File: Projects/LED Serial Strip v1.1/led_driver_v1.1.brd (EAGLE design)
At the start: 64.5 x 53.3 mm, 97 parts, among them U1 TLC5947DAP, U2 TLC5947DAP, U3 74LS595D, U4 UDN2982SLW, U5 74LS595D, U6 UDN2982SLW, U7 ARDUINO_R3_SHIELD

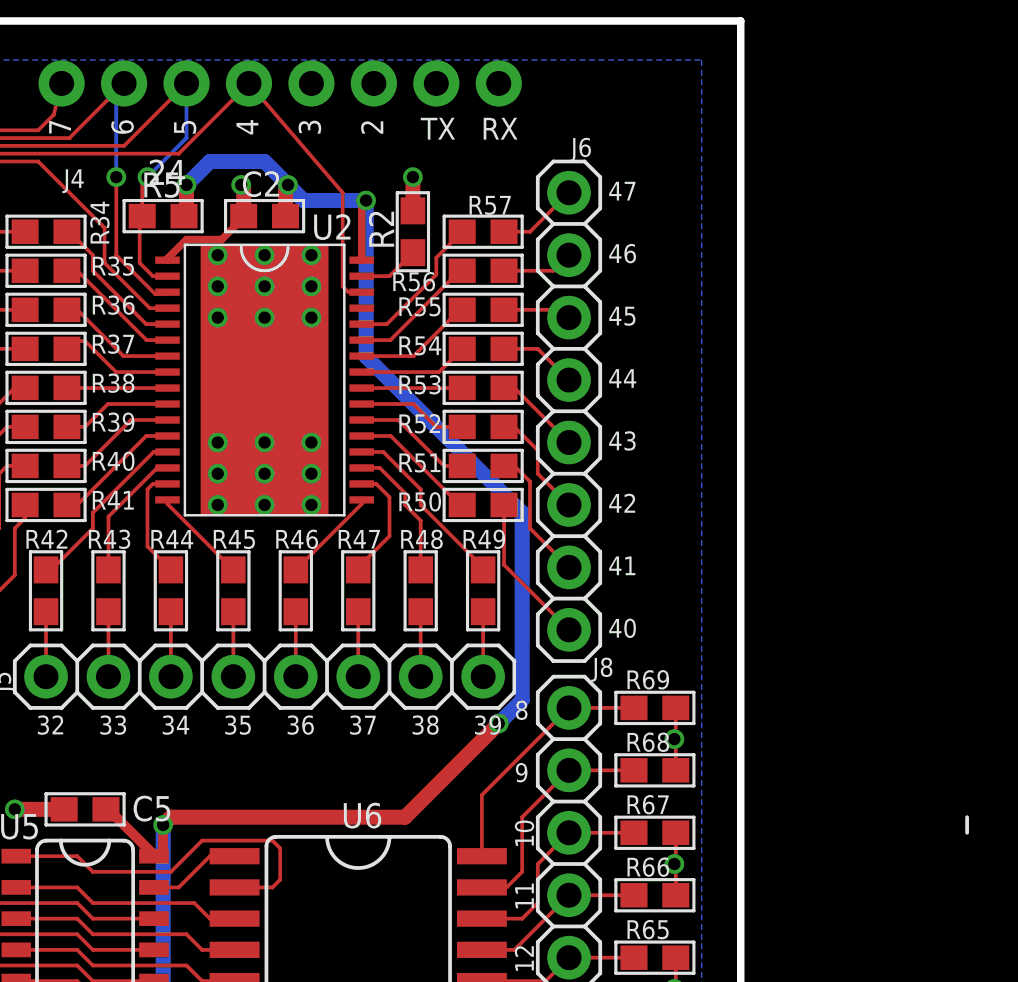
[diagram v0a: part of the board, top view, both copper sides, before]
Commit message: 
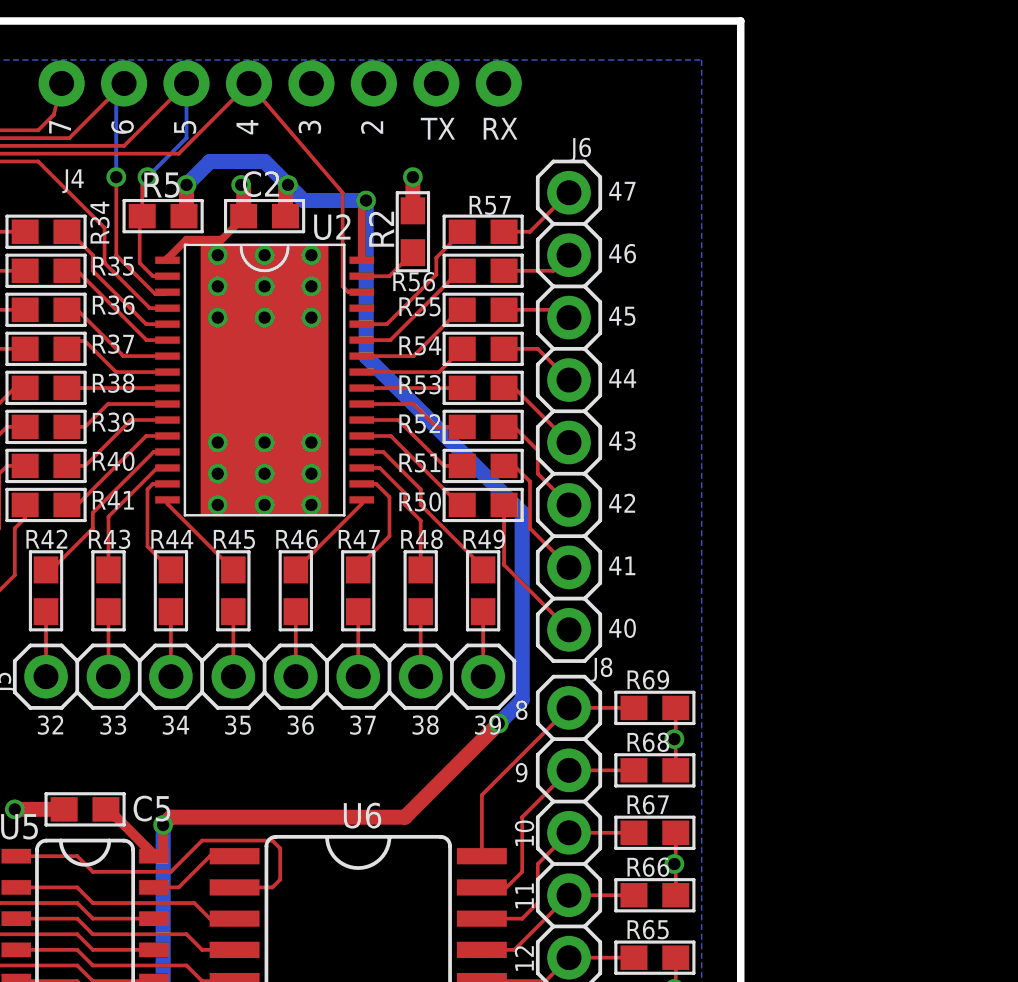
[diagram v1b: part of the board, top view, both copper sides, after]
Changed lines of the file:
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@@
 <?xml version="1.0" encoding="utf-8"?>
 <!DOCTYPE eagle SYSTEM "eagle.dtd">
-<eagle version="6.5.0">
+<eagle version="7.1.0">
 <drawing>
 <settings>
@@
 <grid distance="0.0125" unitdist="inch" unit="inch" style="lines" multiple="1" display="yes" altdistance="0.00625" altunitdist="inch" altunit="inch"/>
 <layers>
-<layer number="1" name="Top" color="4" fill="1" visible="yes" active="yes"/>
-<layer number="16" name="Bottom" color="1" fill="1" visible="yes" active="yes"/>
+<layer number="1" name="Top" color="4" fill="1" visible="no" active="yes"/>
+<layer number="16" name="Bottom" color="1" fill="1" visible="no" active="yes"/>
 <layer number="17" name="Pads" color="2" fill="1" visible="yes" active="yes"/>
-<layer number="18" name="Vias" color="2" fill="1" visible="yes" active="yes"/>
-<layer number="19" name="Unrouted" color="14" fill="1" visible="yes" active="yes"/>
+<layer number="18" name="Vias" color="2" fill="1" visible="no" active="yes"/>
+<layer number="19" name="Unrouted" color="14" fill="1" visible="no" active="yes"/>
 <layer number="20" name="Dimension" color="15" fill="1" visible="yes" active="yes"/>
 <layer number="21" name="tPlace" color="6" fill="1" visible="yes" active="yes"/>
 <layer number="22" name="bPlace" color="5" fill="1" visible="no" active="yes"/>
-<layer number="23" name="tOrigins" color="15" fill="1" visible="yes" active="yes"/>
+<layer number="23" name="tOrigins" color="15" fill="1" visible="no" active="yes"/>
 <layer number="24" name="bOrigins" color="15" fill="1" visible="no" active="yes"/>
 <layer number="25" name="tNames" color="13" fill="1" visible="yes" active="yes"/>
@@
 <text x="12.3825" y="5.715" size="1.016" layer="25" font="vector" ratio="15" rot="R180" align="top-left">VIN1</text>
 <text x="15.875" y="5.715" size="1.016" layer="25" font="vector" ratio="15" rot="R180" align="top-left">VIN2</text>
-<text x="40.3225" y="46.6725" size="1.016" layer="25" font="vector" ratio="15">24</text>
 <text x="57.785" y="2.2225" size="1.27" layer="25" font="vector" ratio="15" rot="R90">SDA</text>
 <text x="64.135" y="2.2225" size="1.27" layer="25" font="vector" ratio="15" rot="R90">SCL</text>
-<wire x1="73.66" y1="20.32" x2="73.66" y2="20.955" width="0.1524" layer="25"/>
 </plain>
 <attributes>
@@
 <pass name="Default">
 <param name="RoutingGrid" value="50mil"/>
+<param name="AutoGrid" value="1"/>
+<param name="Efforts" value="0"/>
+<param name="TopRouterVariant" value="1"/>
 <param name="tpViaShape" value="round"/>
 <param name="PrefDir.1" value="|"/>
